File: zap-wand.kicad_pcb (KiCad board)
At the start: 2 copper layers, 12 x 20 mm, 15 parts, among them IC1 NC7WZ02, Q1 Q_PMOS_GDS, SW1 SW_PUSH_SMALL, U1 NCP4683DSQ33T1G

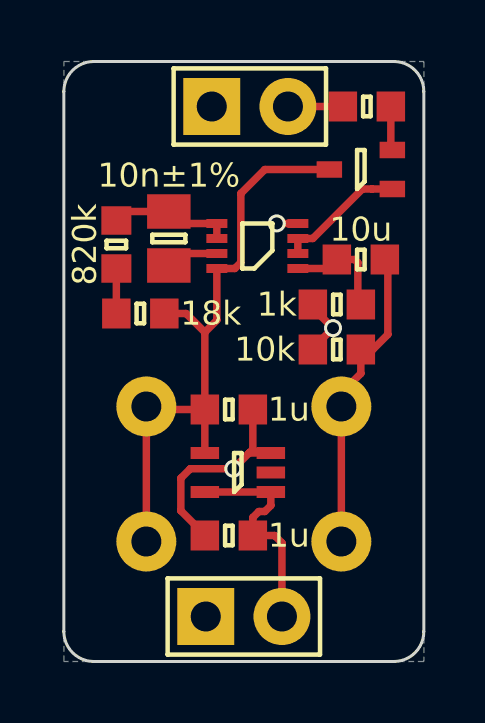
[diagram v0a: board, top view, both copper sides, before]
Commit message: Added xor output inverter
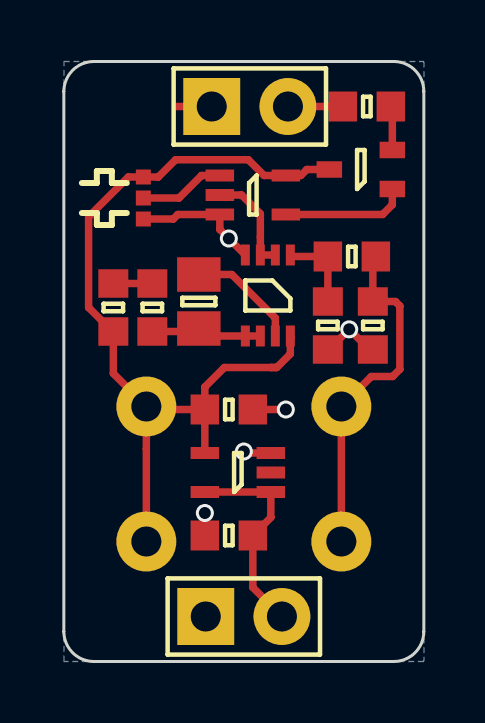
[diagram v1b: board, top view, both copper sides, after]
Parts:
- added IC2: NC7SZ86, agg:SC-70-5, F.Cu at (66.3, 34.5)
- added JP1: JUMPER3, parts:solder_jumper_3, F.Cu at (62.6, 33.9)
- moved R2 2.42 mm to (63.0, 38.2), turned to 270 degrees
- moved C2 2.33 mm to (64.5, 38.0), turned to 90 degrees
- moved IC1 1.69 mm to (66.8, 37.8), turned to 270 degrees
- moved R4 1.44 mm to (70.3, 38.8), turned to 90 degrees
- moved R5 0.92 mm to (61.6, 38.2), turned to 90 degrees
- moved R1 0.76 mm to (68.8, 38.8), turned to 90 degrees
- moved C1 0.32 mm to (69.6, 36.5)
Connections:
- Q1 pad 1: Net-(IC1-Pad2) -> Net-(IC2-Pad4)
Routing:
- net +3V3: track 20.9 -> 29.1 mm
- net Net-(IC2-Pad4): track 0.00 -> 4.21 mm
- net Net-(IC2-Pad1): track 0.00 -> 2.86 mm
- net Net-(C2-Pad2): track 1.77 -> 3.75 mm
- net Net-(IC1-Pad2): track 4.48 -> 3.48 mm
- net Net-(C1-Pad1): track 3.61 -> 2.77 mm
- net Net-(BATT1-Pad1): track 7.54 -> 7.00 mm
- net Net-(C1-Pad2): track 11.1 -> 11.6 mm
- net GND: track 9.85 -> 10.3 mm, vias 3 -> 5
